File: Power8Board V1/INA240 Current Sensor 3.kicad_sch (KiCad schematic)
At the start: 3 parts, among them U6 INA240A2PWR

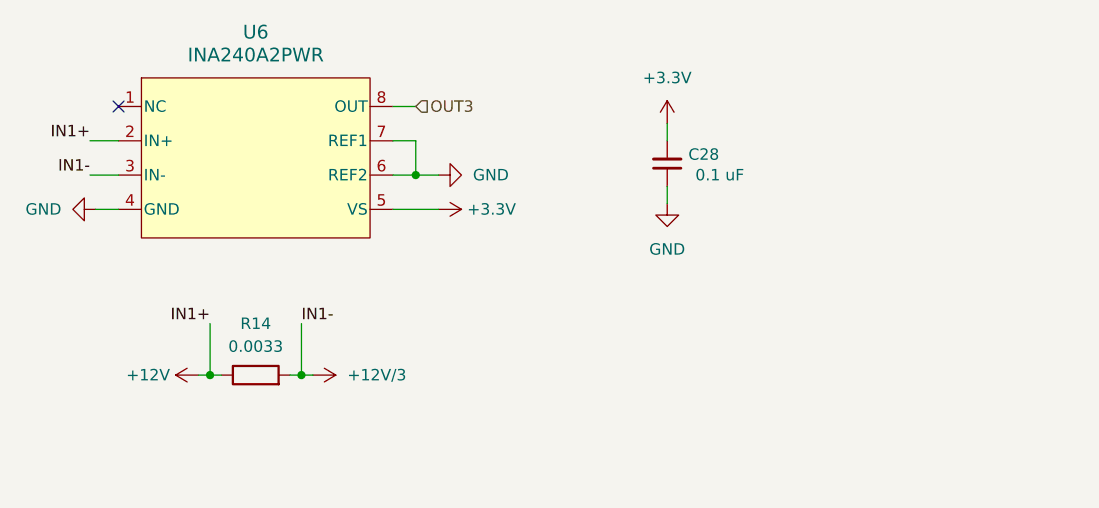
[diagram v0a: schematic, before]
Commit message: Laid out components
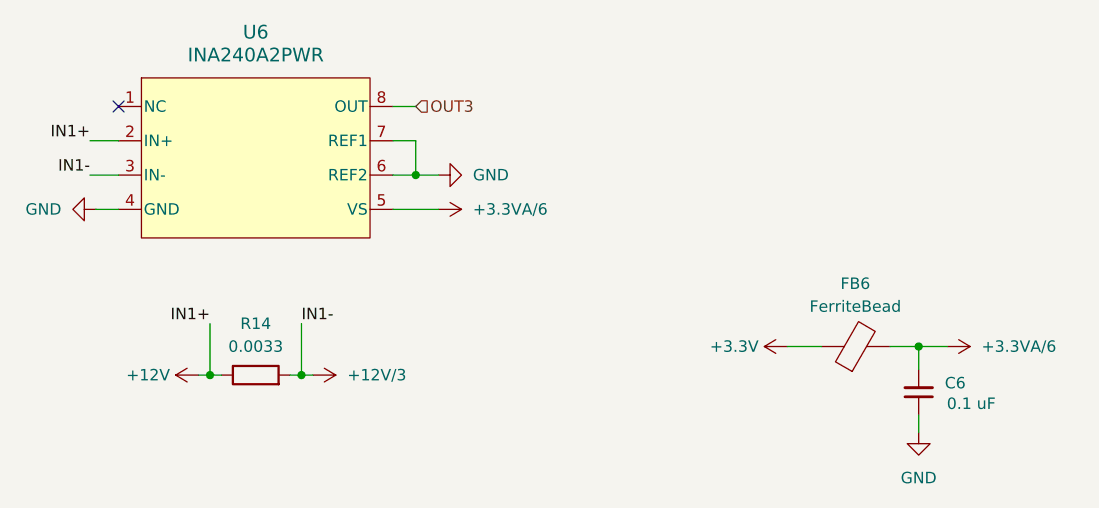
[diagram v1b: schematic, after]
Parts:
- removed C28: 0.1 uF, 0805 Ceramic Capacitor:CAPC2012X140N, symbol Device:C_Small
- added C6: 0.1 uF, 0805 Ceramic Capacitor:CAPC2012X140N, symbol Device:C_Small
- added FB6: FerriteBead, MPZ2012S102ATD25:BEADC2012X105N, symbol Device:FerriteBead
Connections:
- net +3.3V: now also FB6.1; no longer U6.5 (VS)
- net GND: now also C6.1
- new net +3.3VA/6: C6.2, FB6.2, U6.5 (VS)
